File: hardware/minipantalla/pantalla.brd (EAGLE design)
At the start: 38.5 x 51 mm, 4 parts

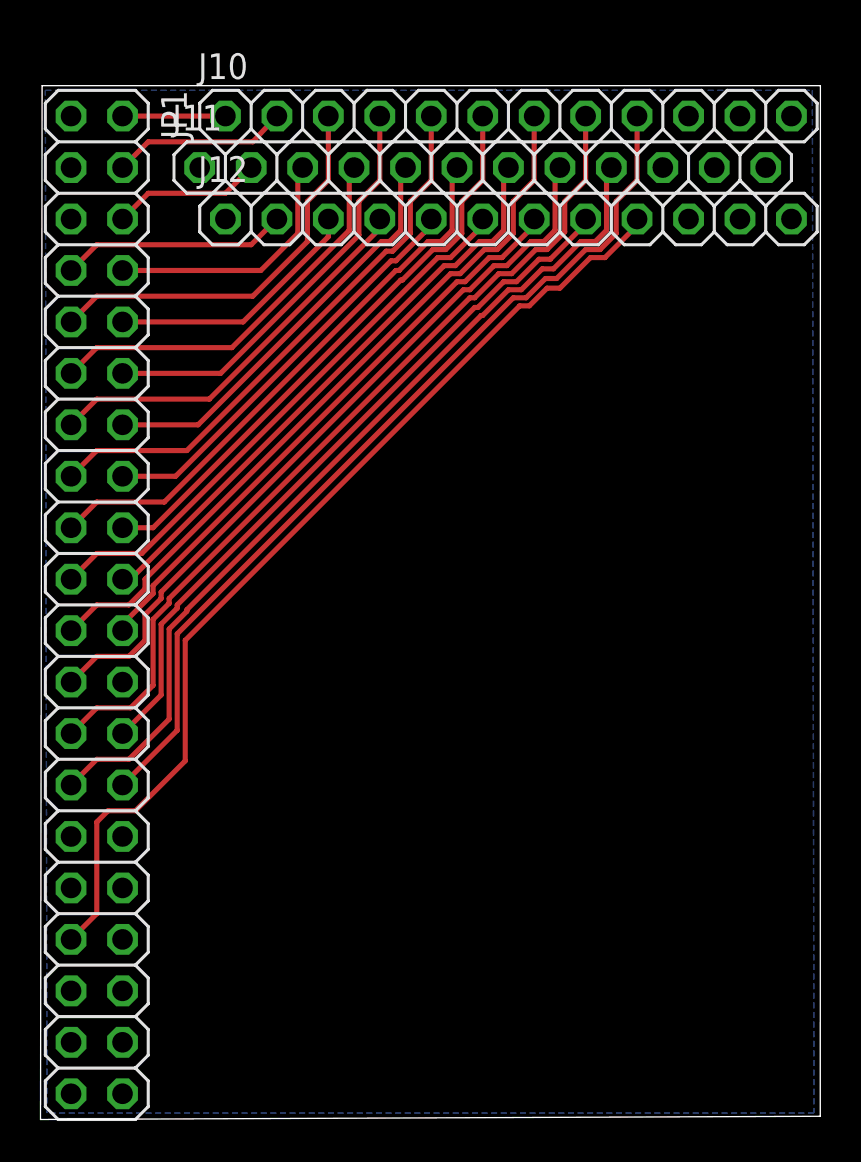
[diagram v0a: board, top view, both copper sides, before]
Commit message: Finalizo pantalla
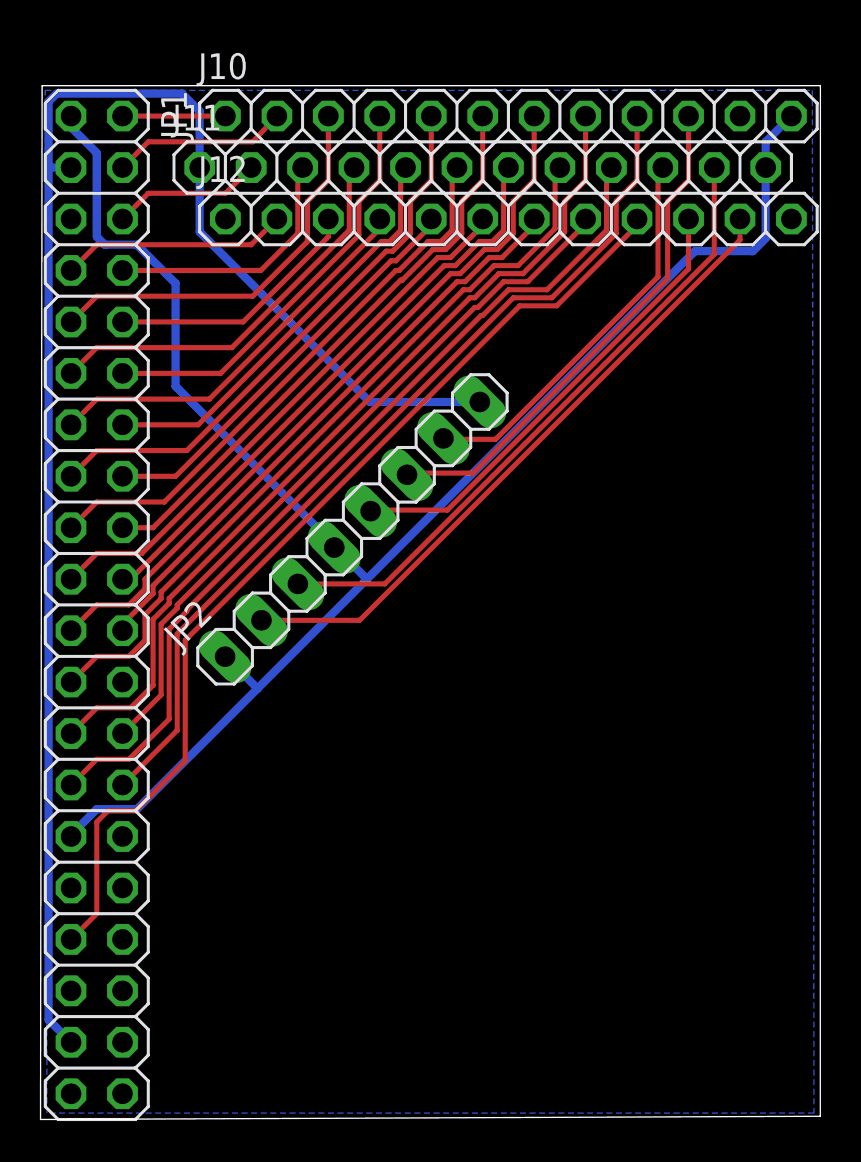
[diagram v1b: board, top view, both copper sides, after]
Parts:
- added JP2: (no value), pinhead:1X08
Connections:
- net 3.3V: now also JP2.8; no longer J12.12
- net GND: now also JP2.1, JP2.4
- net P12: now also JP2.3
- net P14: now also JP2.2
- net P15: now also JP2.6
- net P16: now also JP2.7
- net P17: now also JP2.5
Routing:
- net GND: track 0.00 -> 85.2 mm
- net 3.3V: track 0.00 -> 79.3 mm
- net P14: track 0.00 -> 32.4 mm
- net P12: track 0.00 -> 31.6 mm
- net P15: track 0.00 -> 25.3 mm
- net P17: track 0.00 -> 23.1 mm
- net P16: track 0.00 -> 19.4 mm
